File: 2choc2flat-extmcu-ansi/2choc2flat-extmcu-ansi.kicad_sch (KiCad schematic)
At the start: 140 parts, among them K1 KEYSW, K10 KEYSW, K11 KEYSW, K12 KEYSW, K13 KEYSW, K14 KEYSW, K16 KEYSW, K17 KEYSW, K18 KEYSW, K19 KEYSW, K2 KEYSW, K20 KEYSW, K21 KEYSW, K22 KEYSW, K23 KEYSW, K24 KEYSW, K25 KEYSW, K26 KEYSW, K27 KEYSW, K28 KEYSW, K29 KEYSW, K3 KEYSW, K31 KEYSW, K31-1 KEYSW, K32 KEYSW, K33 KEYSW, K34 KEYSW, K35 KEYSW, K36 KEYSW, K37 KEYSW, K38 KEYSW, K39 KEYSW, K4 KEYSW, K40 KEYSW, K41 KEYSW, K42 KEYSW, K44 KEYSW, K46 KEYSW, K47 KEYSW, K48 KEYSW, K49 KEYSW, K5 KEYSW, K50 KEYSW, K51 KEYSW, K52 KEYSW, K53 KEYSW, K54 KEYSW, K55 KEYSW, K56 KEYSW, K57 KEYSW, K58 KEYSW, K59 KEYSW, K6 KEYSW, K61 KEYSW, K62 KEYSW, K63 KEYSW, K67 KEYSW, K7 KEYSW, K71 KEYSW, K72 KEYSW, K73 KEYSW, K74 KEYSW, K75 KEYSW, K8 KEYSW, K9 KEYSW, U1 WS-RP2040-Tiny

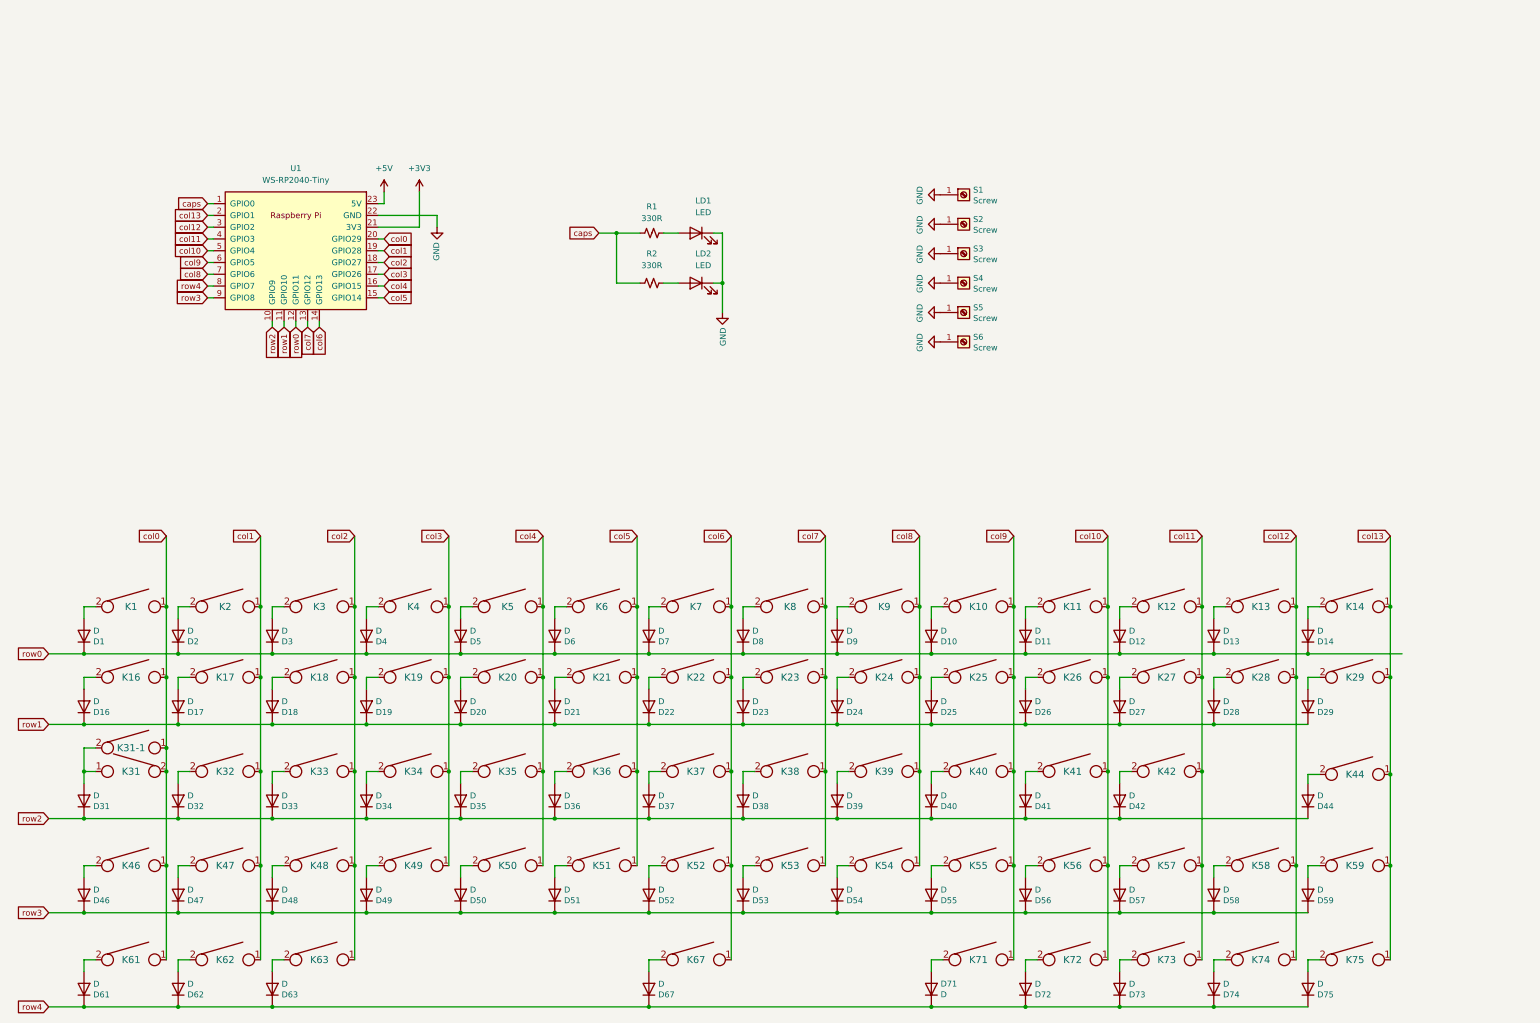
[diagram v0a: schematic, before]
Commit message: wip adding RGB lighting
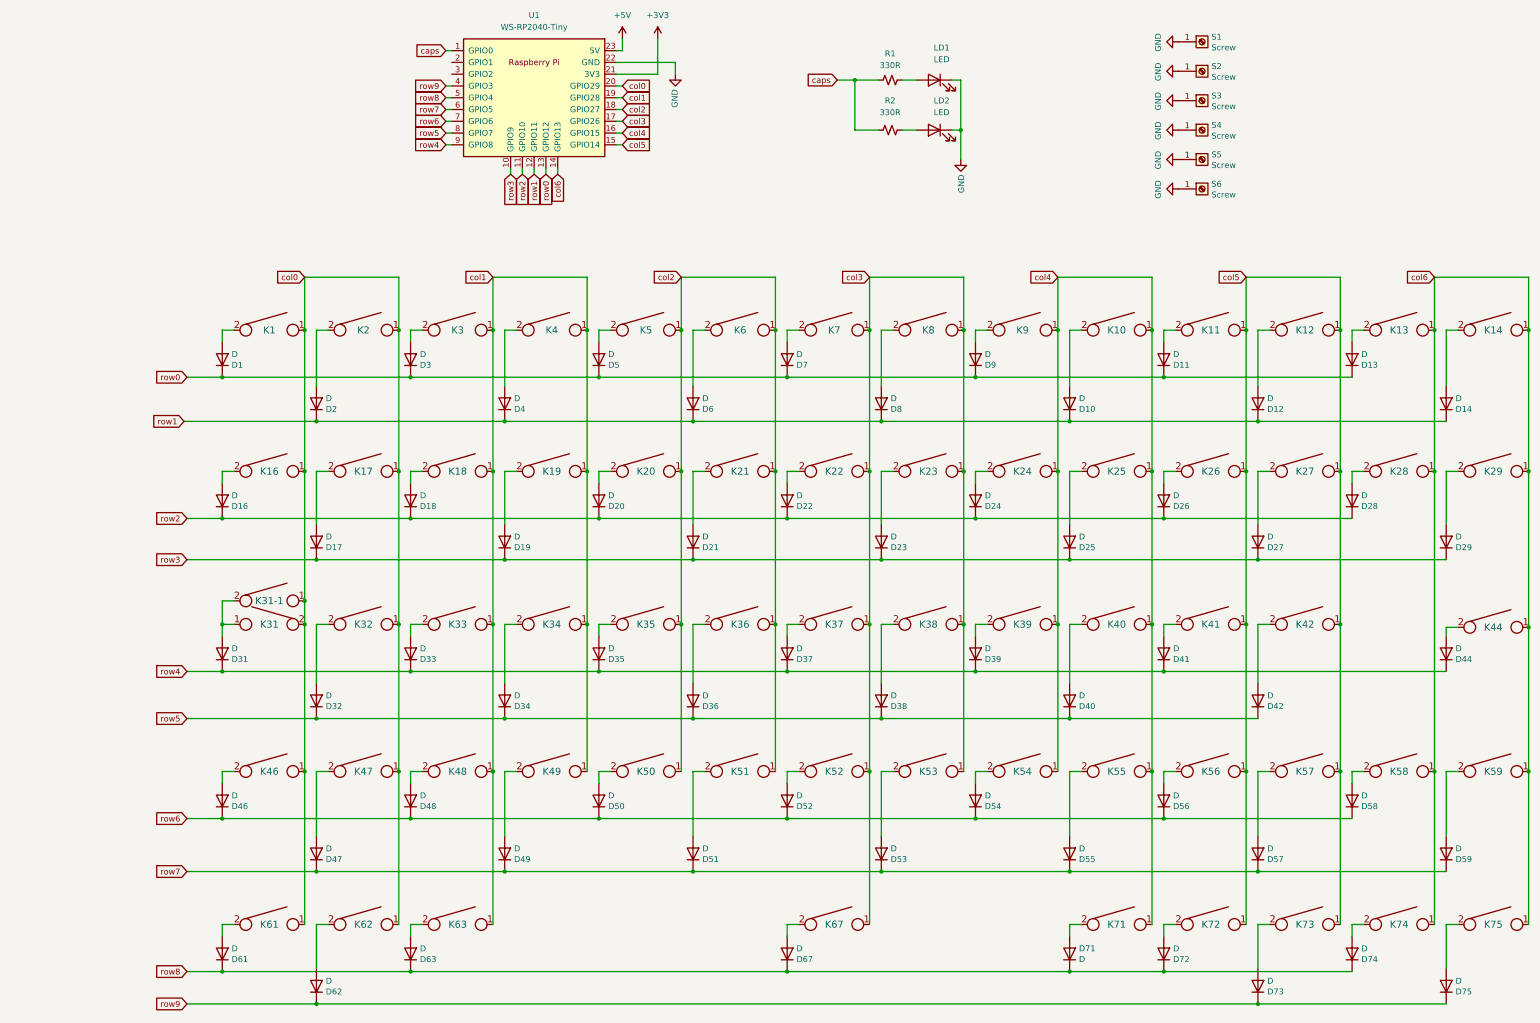
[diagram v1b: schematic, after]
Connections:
- net col0: now also K17.1, K2.1, K32.1, K47.1, K62.1
- net col1: now also K18.1, K19.1, K3.1, K33.1, K34.1, K4.1, K48.1, K49.1, K63.1; no longer K17.1, K2.1, K32.1, K47.1, K62.1
- net col2: now also K20.1, K21.1, K35.1, K36.1, K5.1, K50.1, K51.1, K6.1; no longer K18.1, K3.1, K33.1, K48.1, K63.1
- net col3: now also K22.1, K23.1, K37.1, K38.1, K52.1, K53.1, K67.1, K7.1, K8.1; no longer K19.1, K34.1, K4.1, K49.1
- net col4: now also K10.1, K24.1, K25.1, K39.1, K40.1, K54.1, K55.1, K71.1, K9.1; no longer K20.1, K35.1, K5.1, K50.1
- net col5: now also K11.1, K12.1, K26.1, K27.1, K41.1, K42.1, K56.1, K57.1, K72.1, K73.1; no longer K21.1, K36.1, K51.1, K6.1
- net col6: now also K13.1, K14.1, K28.1, K29.1, K44.1, K58.1, K59.1, K74.1, K75.1; no longer K22.1, K37.1, K52.1, K67.1, K7.1
- net row0: now also U1.13 (GPIO12); no longer D10.1 (K), D12.1 (K), D14.1 (K), D2.1 (K), D4.1 (K), D6.1 (K), D8.1 (K), U1.12 (GPIO11)
- net row1: now also D10.1 (K), D12.1 (K), D14.1 (K), D2.1 (K), D4.1 (K), D6.1 (K), D8.1 (K), U1.12 (GPIO11); no longer D16.1 (K), D17.1 (K), D18.1 (K), D19.1 (K), D20.1 (K), D21.1 (K), D22.1 (K), D23.1 (K), D24.1 (K), D25.1 (K), D26.1 (K), D27.1 (K), D28.1 (K), D29.1 (K), U1.11 (GPIO10)
- net row2: now also D16.1 (K), D18.1 (K), D20.1 (K), D22.1 (K), D24.1 (K), D26.1 (K), D28.1 (K), U1.11 (GPIO10); no longer D31.1 (K), D32.1 (K), D33.1 (K), D34.1 (K), D35.1 (K), D36.1 (K), D37.1 (K), D38.1 (K), D39.1 (K), D40.1 (K), D41.1 (K), D42.1 (K), D44.1 (K), U1.10 (GPIO9)
- net row3: now also D17.1 (K), D19.1 (K), D21.1 (K), D23.1 (K), D25.1 (K), D27.1 (K), D29.1 (K), U1.10 (GPIO9); no longer D46.1 (K), D47.1 (K), D48.1 (K), D49.1 (K), D50.1 (K), D51.1 (K), D52.1 (K), D53.1 (K), D54.1 (K), D55.1 (K), D56.1 (K), D57.1 (K), D58.1 (K), D59.1 (K), U1.9 (GPIO8)
- net row4: now also D31.1 (K), D33.1 (K), D35.1 (K), D37.1 (K), D39.1 (K), D41.1 (K), D44.1 (K), U1.9 (GPIO8); no longer D61.1 (K), D62.1 (K), D63.1 (K), D67.1 (K), D71.1 (K), D72.1 (K), D73.1 (K), D74.1 (K), D75.1 (K), U1.8 (GPIO7)
- removed net col10: K11.1, K26.1, K41.1, K56.1, K72.1, U1.5 (GPIO4)
- removed net col11: K12.1, K27.1, K42.1, K57.1, K73.1, U1.4 (GPIO3)
- removed net col12: K13.1, K28.1, K58.1, K74.1, U1.3 (GPIO2)
- removed net col13: K14.1, K29.1, K44.1, K59.1, K75.1, U1.2 (GPIO1)
- removed net col7: K23.1, K38.1, K53.1, K8.1, U1.13 (GPIO12)
- removed net col8: K24.1, K39.1, K54.1, K9.1, U1.7 (GPIO6)
- removed net col9: K10.1, K25.1, K40.1, K55.1, K71.1, U1.6 (GPIO5)
- new net row5: D32.1 (K), D34.1 (K), D36.1 (K), D38.1 (K), D40.1 (K), D42.1 (K), U1.8 (GPIO7)
- new net row6: D46.1 (K), D48.1 (K), D50.1 (K), D52.1 (K), D54.1 (K), D56.1 (K), D58.1 (K), U1.7 (GPIO6)
- new net row7: D47.1 (K), D49.1 (K), D51.1 (K), D53.1 (K), D55.1 (K), D57.1 (K), D59.1 (K), U1.6 (GPIO5)
- new net row8: D61.1 (K), D63.1 (K), D67.1 (K), D71.1 (K), D72.1 (K), D74.1 (K), U1.5 (GPIO4)
- new net row9: D62.1 (K), D73.1 (K), D75.1 (K), U1.4 (GPIO3)
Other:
- moved on the sheet: D1, D10, D11, D12, D13, D14, D16, D17, D18, D19, D2, D20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

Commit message: restore non-RGB versions from history into separate dirs
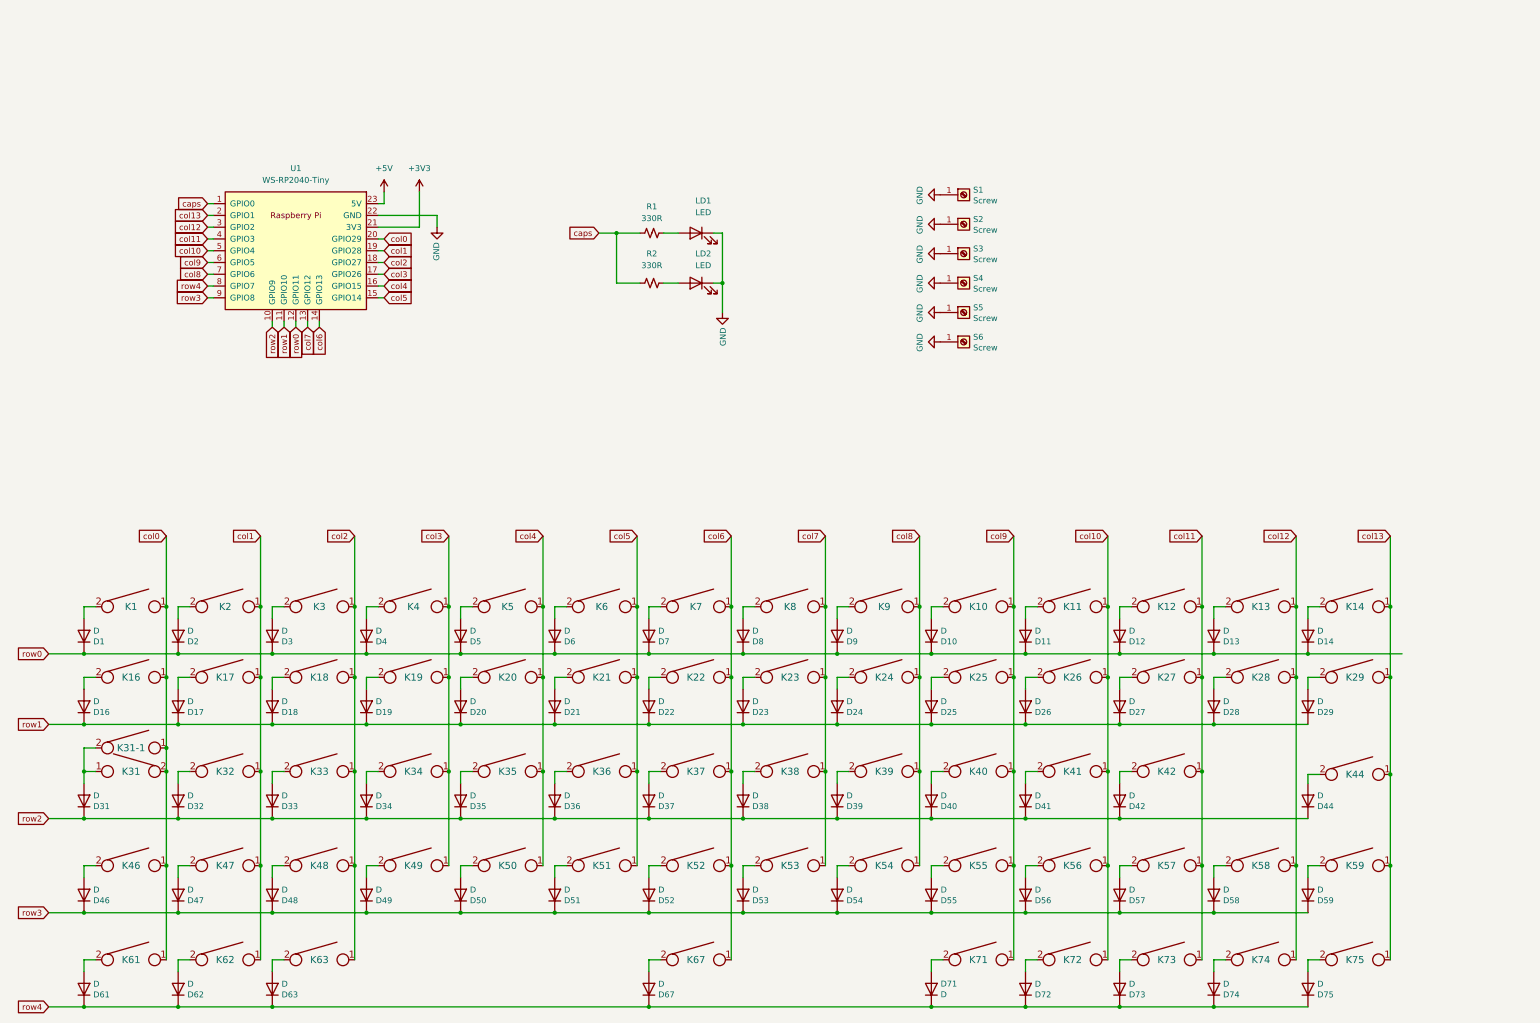
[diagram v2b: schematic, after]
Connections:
- net col0: no longer K17.1, K2.1, K32.1, K47.1, K62.1
- net col1: now also K17.1, K2.1, K32.1, K47.1, K62.1; no longer K18.1, K19.1, K3.1, K33.1, K34.1, K4.1, K48.1, K49.1, K63.1
- net col2: now also K18.1, K3.1, K33.1, K48.1, K63.1; no longer K20.1, K21.1, K35.1, K36.1, K5.1, K50.1, K51.1, K6.1
- net col3: now also K19.1, K34.1, K4.1, K49.1; no longer K22.1, K23.1, K37.1, K38.1, K52.1, K53.1, K67.1, K7.1, K8.1
- net col4: now also K20.1, K35.1, K5.1, K50.1; no longer K10.1, K24.1, K25.1, K39.1, K40.1, K54.1, K55.1, K71.1, K9.1
- net col5: now also K21.1, K36.1, K51.1, K6.1; no longer K11.1, K12.1, K26.1, K27.1, K41.1, K42.1, K56.1, K57.1, K72.1, K73.1
- net col6: now also K22.1, K37.1, K52.1, K67.1, K7.1; no longer K13.1, K14.1, K28.1, K29.1, K44.1, K58.1, K59.1, K74.1, K75.1
- net row0: now also D10.1 (K), D12.1 (K), D14.1 (K), D2.1 (K), D4.1 (K), D6.1 (K), D8.1 (K), U1.12 (GPIO11); no longer U1.13 (GPIO12)
- net row1: now also D16.1 (K), D17.1 (K), D18.1 (K), D19.1 (K), D20.1 (K), D21.1 (K), D22.1 (K), D23.1 (K), D24.1 (K), D25.1 (K), D26.1 (K), D27.1 (K), D28.1 (K), D29.1 (K), U1.11 (GPIO10); no longer D10.1 (K), D12.1 (K), D14.1 (K), D2.1 (K), D4.1 (K), D6.1 (K), D8.1 (K), U1.12 (GPIO11)
- net row2: now also D31.1 (K), D32.1 (K), D33.1 (K), D34.1 (K), D35.1 (K), D36.1 (K), D37.1 (K), D38.1 (K), D39.1 (K), D40.1 (K), D41.1 (K), D42.1 (K), D44.1 (K), U1.10 (GPIO9); no longer D16.1 (K), D18.1 (K), D20.1 (K), D22.1 (K), D24.1 (K), D26.1 (K), D28.1 (K), U1.11 (GPIO10)
- net row3: now also D46.1 (K), D47.1 (K), D48.1 (K), D49.1 (K), D50.1 (K), D51.1 (K), D52.1 (K), D53.1 (K), D54.1 (K), D55.1 (K), D56.1 (K), D57.1 (K), D58.1 (K), D59.1 (K), U1.9 (GPIO8); no longer D17.1 (K), D19.1 (K), D21.1 (K), D23.1 (K), D25.1 (K), D27.1 (K), D29.1 (K), U1.10 (GPIO9)
- net row4: now also D61.1 (K), D62.1 (K), D63.1 (K), D67.1 (K), D71.1 (K), D72.1 (K), D73.1 (K), D74.1 (K), D75.1 (K), U1.8 (GPIO7); no longer D31.1 (K), D33.1 (K), D35.1 (K), D37.1 (K), D39.1 (K), D41.1 (K), D44.1 (K), U1.9 (GPIO8)
- net col13: now reaches U1.2 (GPIO1)
- net col13: now also K14.1, K29.1, K44.1, K59.1, K75.1
- net col12: now reaches U1.3 (GPIO2)
- net col12: now also K13.1, K28.1, K58.1, K74.1
- removed net row5: D32.1 (K), D34.1 (K), D36.1 (K), D38.1 (K), D40.1 (K), D42.1 (K), U1.8 (GPIO7)
- removed net row6: D46.1 (K), D48.1 (K), D50.1 (K), D52.1 (K), D54.1 (K), D56.1 (K), D58.1 (K), U1.7 (GPIO6)
- removed net row7: D47.1 (K), D49.1 (K), D51.1 (K), D53.1 (K), D55.1 (K), D57.1 (K), D59.1 (K), U1.6 (GPIO5)
- removed net row8: D61.1 (K), D63.1 (K), D67.1 (K), D71.1 (K), D72.1 (K), D74.1 (K), U1.5 (GPIO4)
- removed net row9: D62.1 (K), D73.1 (K), D75.1 (K), U1.4 (GPIO3)
- new net col10: K11.1, K26.1, K41.1, K56.1, K72.1, U1.5 (GPIO4)
- new net col11: K12.1, K27.1, K42.1, K57.1, K73.1, U1.4 (GPIO3)
- new net col7: K23.1, K38.1, K53.1, K8.1, U1.13 (GPIO12)
- new net col8: K24.1, K39.1, K54.1, K9.1, U1.7 (GPIO6)
- new net col9: K10.1, K25.1, K40.1, K55.1, K71.1, U1.6 (GPIO5)
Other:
- moved on the sheet: D1, D10, D11, D12, D13, D14, D16, D17, D18, D19, D2, D20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
